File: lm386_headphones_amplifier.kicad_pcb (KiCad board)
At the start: 2 copper layers, 62.5 x 33 mm, 16 parts, among them J1 JACK_TRS_3PINS, J2 JACK_TRS_3PINS, P1 USB_B, U1 LM386, U2 LM386

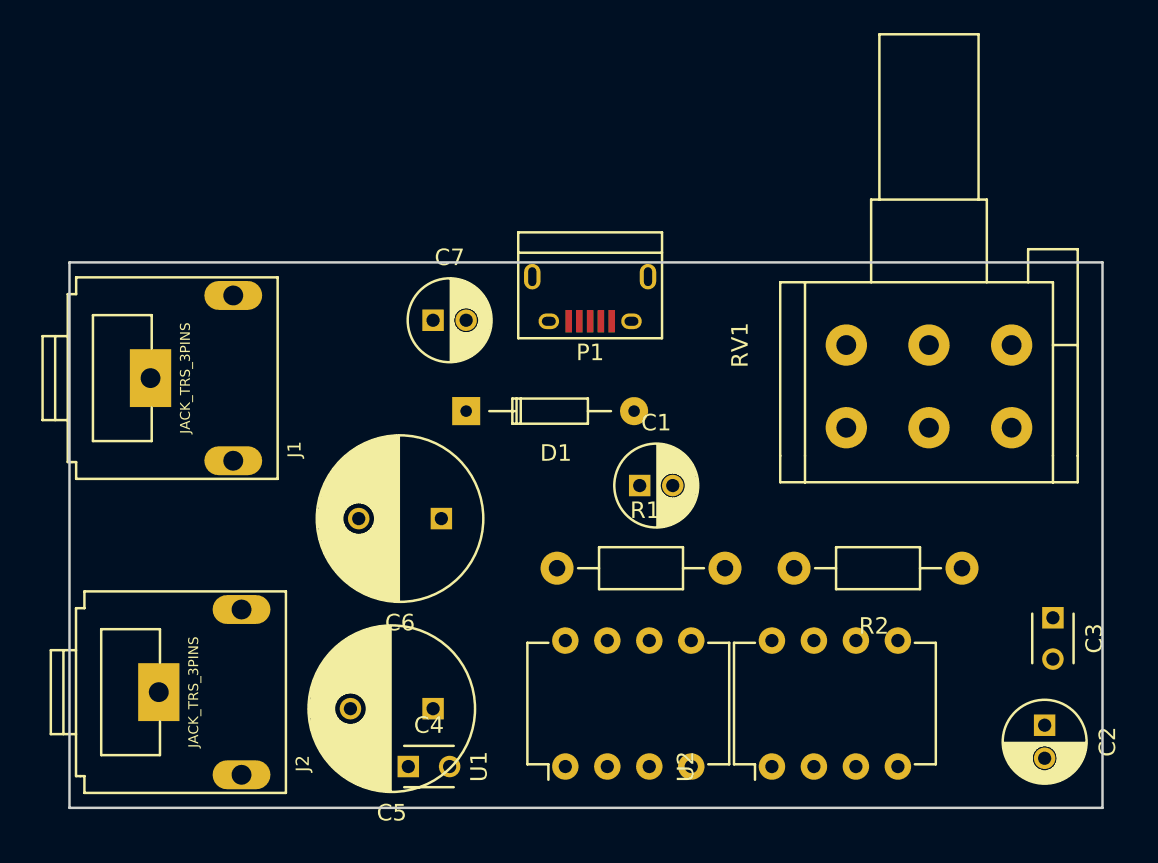
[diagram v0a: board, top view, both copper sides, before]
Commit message: add 100 nF input jack capacitors. Wire the components in pcbnew
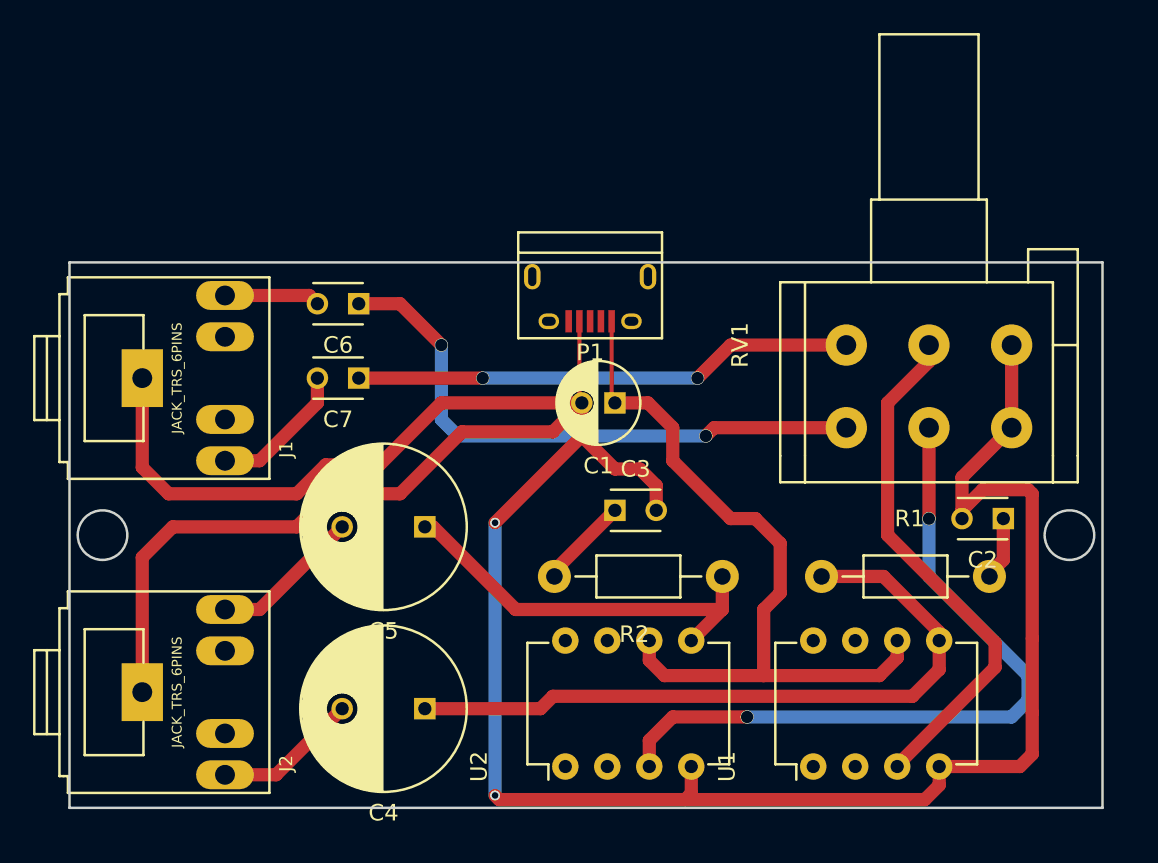
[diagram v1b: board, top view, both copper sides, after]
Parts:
- removed D1: 1N4004, Diodes_ThroughHole:Diode_DO-35_SOD27_Horizontal_RM10
- C2: value 100uF -> 47nF; footprint Capacitors_ThroughHole:C_Radial_D5_L11_P2 -> Capacitors_ThroughHole:C_Disc_D3_P2.5
- C4: value 47nF -> 1000uF; footprint Capacitors_ThroughHole:C_Disc_D3_P2.5 -> Capacitors_ThroughHole:C_Radial_D10_L13_P5
- C6: value 1000uF -> C_Small; footprint Capacitors_ThroughHole:C_Radial_D10_L13_P5 -> Capacitors_ThroughHole:C_Disc_D3_P2.5
- C7: value 100uF -> C_Small; footprint Capacitors_ThroughHole:C_Radial_D5_L11_P2 -> Capacitors_ThroughHole:C_Disc_D3_P2.5
- J1, J2: value JACK_TRS_3PINS -> JACK_TRS_6PINS; footprint audio_connector_3.5mm:3.5mm_stereo_TRS_jack -> minified_lm386_headphones_amplifier:Tayda_3.5mm_stereo_TRS_jack_A-853
- moved C3 27.3 mm to (55.0, 35.0), turned to 0 degrees
- moved R1 16.0 mm to (67.5, 39.0)
- moved U1 15.0 mm to (67.0, 50.5)
- moved R2 14.5 mm to (61.5, 39.0)
- moved C6 13.9 mm to (39.5, 22.5)
- moved C2 12.7 mm to (78.5, 35.5), turned to 180 degrees
- moved U2 12.5 mm to (52.0, 50.5)
- moved C5 11.0 mm to (43.5, 36.0)
- moved C7 5.70 mm to (39.5, 27.0), turned to 180 degrees
- moved C1 5.22 mm to (55.0, 28.5), turned to 180 degrees
- moved C4 3.64 mm to (43.5, 47.0), turned to 180 degrees
- moved J2 1.00 mm to (28.0, 46.0)
- moved J1 0.50 mm to (28.0, 27.0)
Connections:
- C1 pad 1: Net-(C1-Pad1) -> Vcc
- C4 pad 2: GND -> Net-(C4-Pad2)
- C7 pad 1: Vcc -> Net-(C7-Pad1)
- C7 pad 2: GND -> Net-(C7-Pad2)
- J1 pad 2: Net-(J1-Pad2) -> Net-(C6-Pad2)
- J1 pad 3: Net-(J1-Pad3) -> Net-(C7-Pad2)
- J2 pad 2: Net-(C6-Pad2) -> Net-(C5-Pad2)
- J2 pad 3: Net-(C5-Pad2) -> Net-(C4-Pad2)
- P1 pad 1: Net-(D1-Pad2) -> Vcc
- R1 pad 1: Net-(C5-Pad1) -> Net-(C4-Pad1)
- R1 pad 2: Net-(C3-Pad1) -> Net-(C2-Pad1)
- R2 pad 1: Net-(C6-Pad1) -> Net-(C5-Pad1)
- R2 pad 2: Net-(C4-Pad1) -> Net-(C3-Pad1)
- RV1 pad 1: Net-(J1-Pad3) -> Net-(C7-Pad1)
- RV1 pad 4: Net-(J1-Pad2) -> Net-(C6-Pad1)
- U1 pad 5: Net-(C5-Pad1) -> Net-(C4-Pad1)
- U1 pad 7: Net-(C1-Pad1) -> Net-(U1-Pad7)
- U2 pad 5: Net-(C6-Pad1) -> Net-(C5-Pad1)
- U2 pad 7: Net-(C2-Pad1) -> Net-(U2-Pad7)
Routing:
- net GND: track 0.00 -> 181.1 mm, vias 0 -> 2
- net Vcc: track 0.00 -> 46.2 mm
- net Net-(RV1-Pad5): track 0.00 -> 44.5 mm, vias 0 -> 2
- net Net-(C4-Pad1): track 0.00 -> 42.9 mm
- net Net-(C6-Pad1): track 0.00 -> 35.7 mm, vias 0 -> 2
- net Net-(RV1-Pad2): track 0.00 -> 31.7 mm
- net Net-(C7-Pad1): track 0.00 -> 30.3 mm, vias 0 -> 2
- net Net-(C5-Pad1): track 0.00 -> 24.7 mm
- net Net-(C5-Pad2): track 0.00 -> 9.16 mm
- net Net-(C4-Pad2): track 0.00 -> 8.75 mm
- net Net-(C7-Pad2): track 0.00 -> 8.54 mm
- net Net-(C6-Pad2): track 0.00 -> 5.80 mm
- net Net-(C3-Pad1): track 0.00 -> 5.52 mm
- net Net-(C2-Pad1): track 0.00 -> 3.85 mm
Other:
- outline, holes or cut-outs redrawn

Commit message: use large usb type b connector. move stuff around a bit
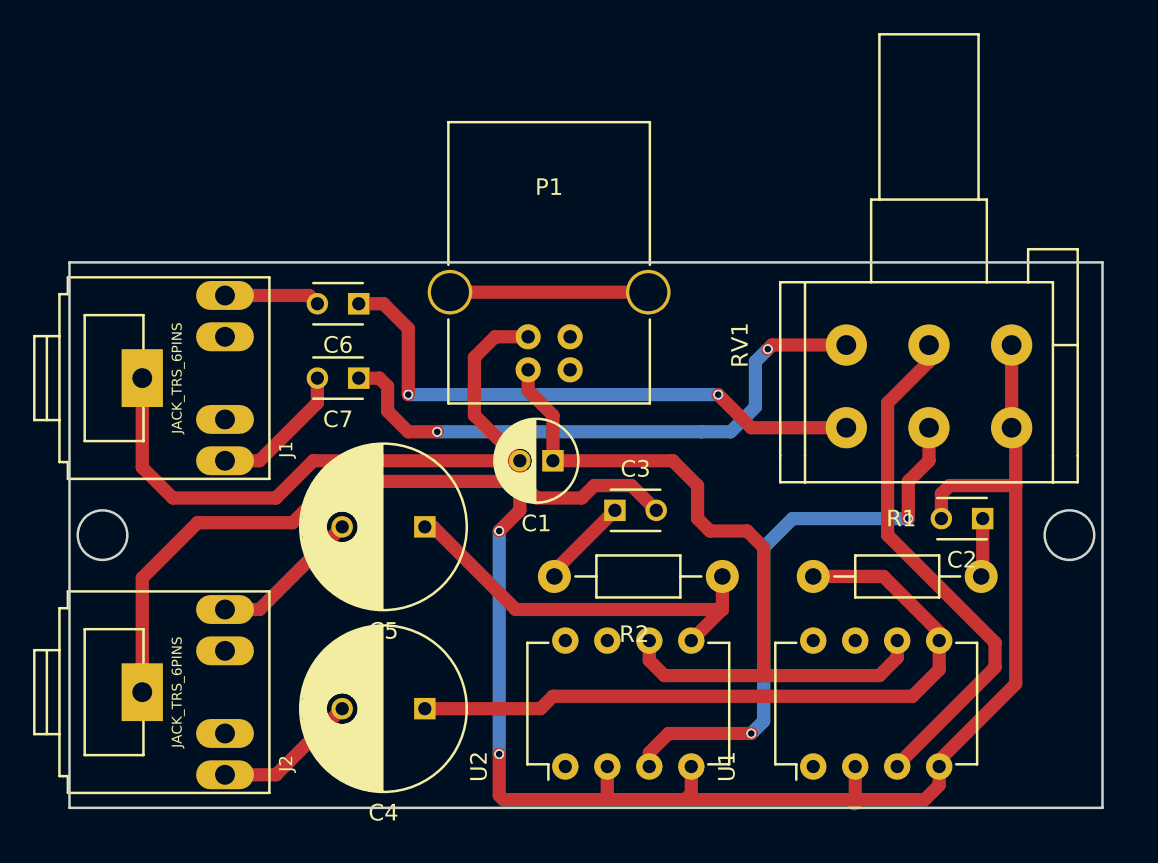
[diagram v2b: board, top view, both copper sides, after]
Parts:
- P1: footprint Connect:USB_Micro-B -> Connect:USB_B
- moved P1 5.86 mm to (49.8, 26.5), turned to 90 degrees
- moved C1 5.13 mm to (51.2, 32.0)
- moved C2 1.25 mm to (77.2, 35.5)
- moved R1 0.50 mm to (67.0, 39.0)
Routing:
- net Net-(P1-Pad5): track 0.00 -> 12.0 mm
- net Net-(RV1-Pad5): track 44.5 -> 34.5 mm
- net GND: track 181.1 -> 174.7 mm
- net Net-(C7-Pad1): track 30.3 -> 35.5 mm
- net Vcc: track 46.2 -> 48.3 mm
- net Net-(C6-Pad1): track 35.7 -> 35.0 mm
- net Net-(C4-Pad1): track 42.9 -> 43.4 mm
